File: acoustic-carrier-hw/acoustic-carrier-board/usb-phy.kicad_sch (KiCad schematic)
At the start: 64 parts, among them J9 TYPE-C-31-M-12, U18 LMV321, U6 TS3USB30EDGSR, U7 USB3300-EZK, Y3 Crystal_GND24_Small

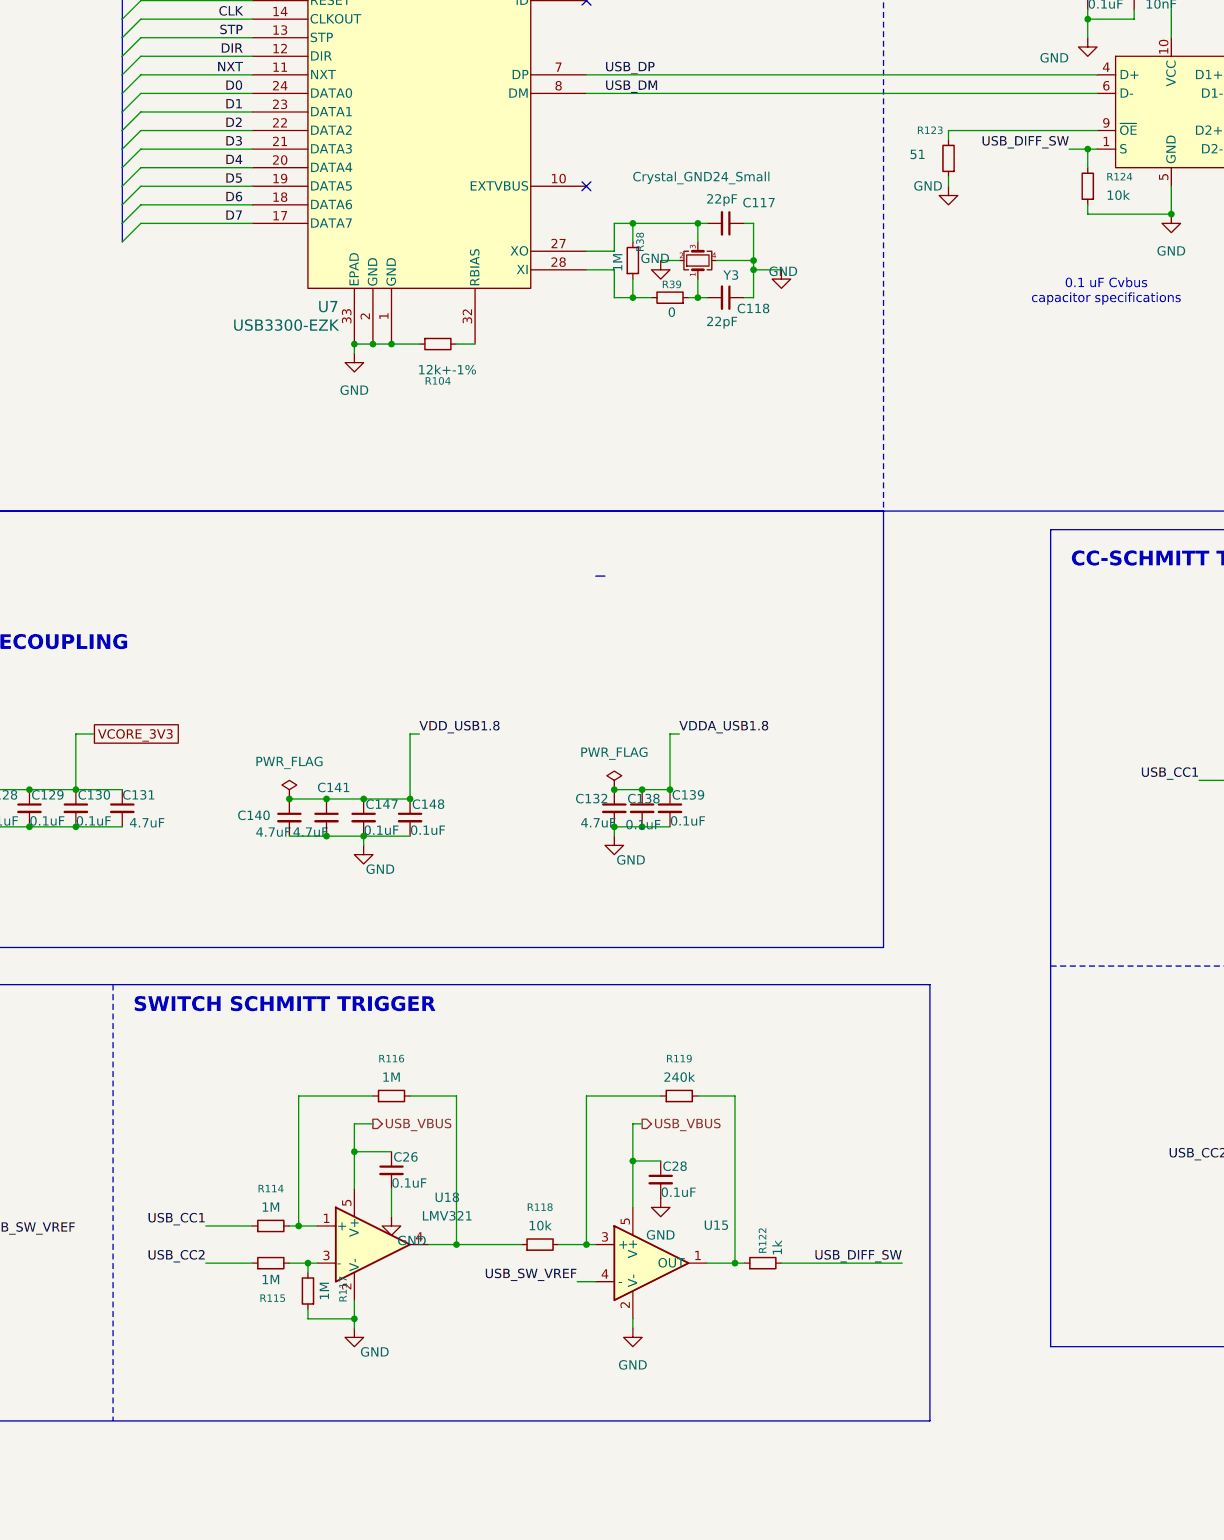
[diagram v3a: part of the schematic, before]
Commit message: [¢arrier] Finished checks, startting with layout and routing
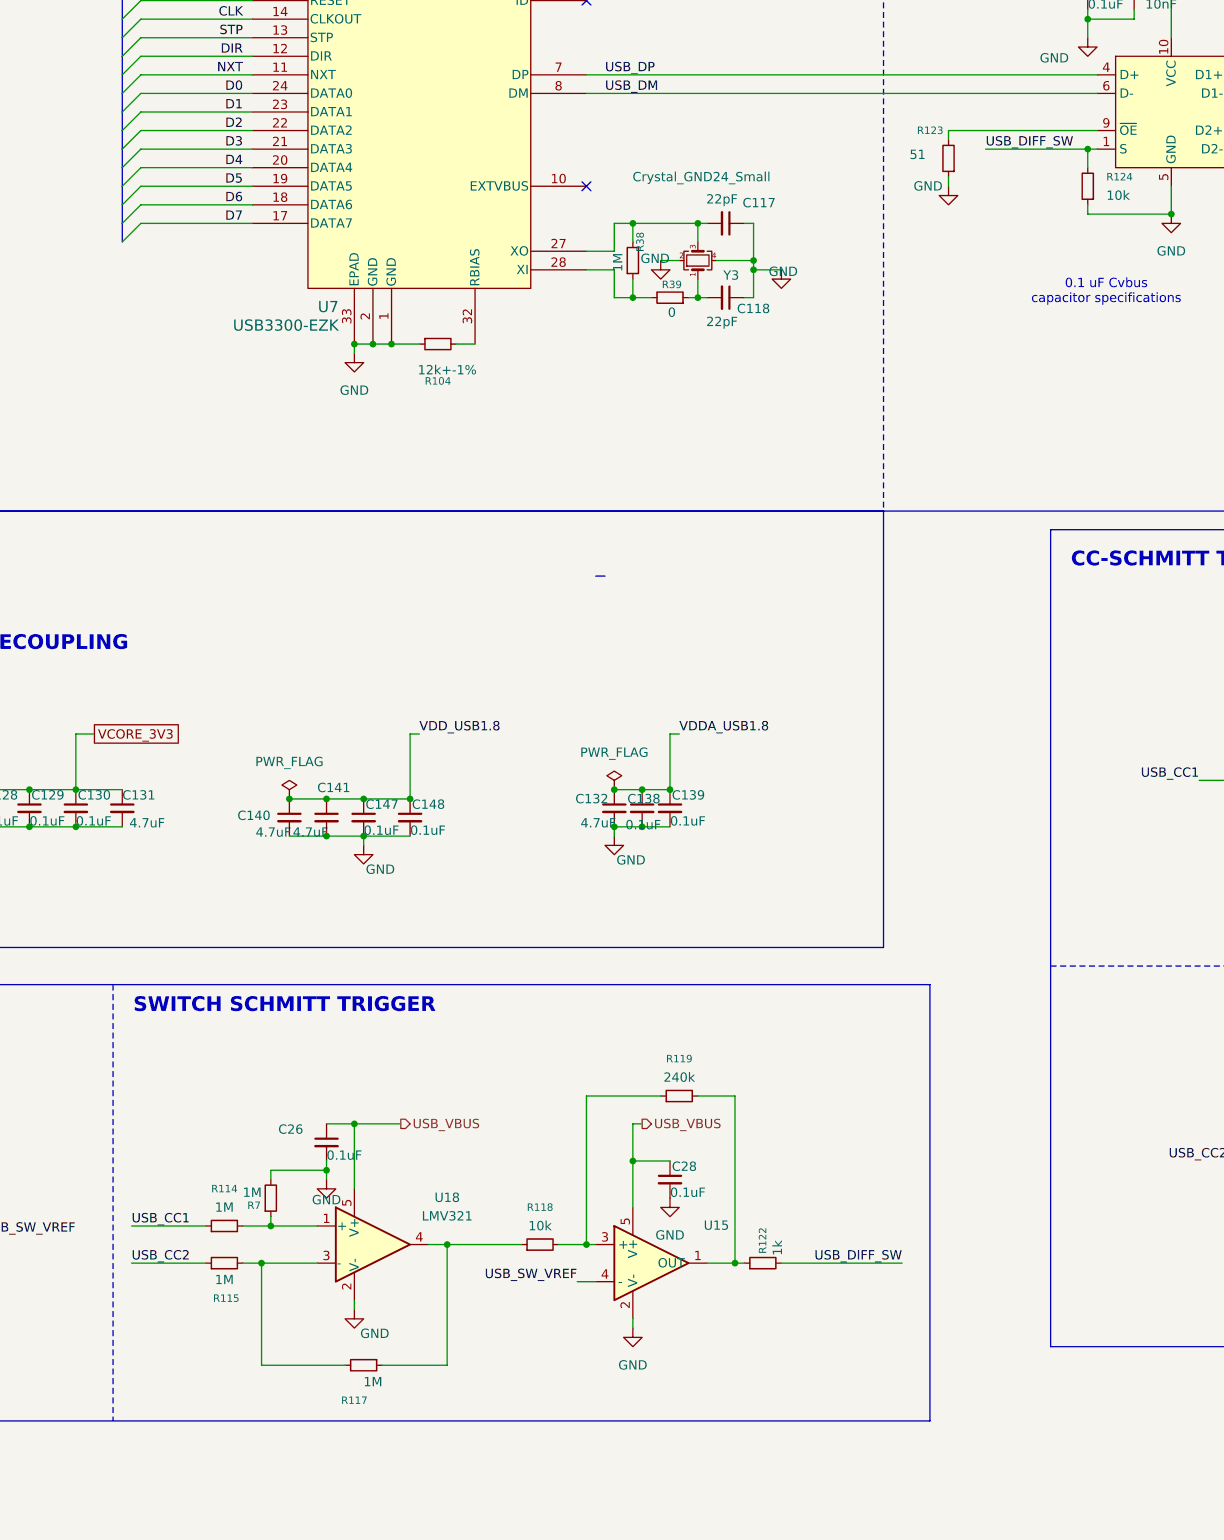
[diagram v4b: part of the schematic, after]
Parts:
- removed R116: 1M, Resistor_SMD:R_0603_1608Metric_Pad0.98x0.95mm_HandSolder, symbol Device:R_Small
- added R7: 1M, Resistor_SMD:R_0603_1608Metric_Pad0.98x0.95mm_HandSolder, symbol Device:R_Small
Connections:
- net GND: now also R7.2; no longer R117.1
- net at R114.2, U18.1 (+): now also R7.1
- net at R118.1, U18.4: now also R117.1
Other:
- moved on the sheet: C26, C28, R114, R115, R117

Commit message: [carrier] Did some check for example schematics, starting layout
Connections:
- net USBDN1 renamed USB_DN1
- net USBDN2 renamed USB_DN2
- net USBDP1 renamed USB_DP1
- net USBDP2 renamed USB_DP2
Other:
- note added: "USB3300 ID PIN: - internally pulled HIGH (peripheral function, USB-B) DP - Termination included where necessary"
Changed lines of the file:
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@@
 		)
 	)
+	(text "USB3300\nID PIN: \n- internally pulled HIGH (peripheral function, USB-B)\nDP\n- Termination included where necessary"
+		(exclude_from_sim no)
+		(at 81.28 38.608 0)
+		(effects
+			(font
+				(size 1.27 1.27)
+			)
+			(justify left bottom)
+		)
+	)
 	(text "USB_CC1: high -> USB_DIFF_SW: high -> D2 ACTIVE\nUSB_CC2: high -> USB_DIFF_SW: low -> D1 ACTIVE"
 		(exclude_from_sim no)
@@
 	)
 	(junction
+		(at 144.78 38.1)
+		(diameter 0)
+		(color 0 0 0 0)
+	)
+	(junction
 		(at 182.88 172.72)
 		(diameter 0)
@@
 	(wire
 		(pts
+			(xy 130.81 38.1) (xy 144.78 38.1)
+		)
+		(stroke
+			(width 0)
+			(type default)
+		)
+	)
+	(wire
+		(pts
 			(xy 88.9 240.03) (xy 88.9 243.84)
 		)
@@
 	(wire
 		(pts
+			(xy 130.81 60.96) (xy 130.81 38.1)
+		)
+		(stroke
+			(width 0)
+			(type default)
+		)
+	)
+	(wire
+		(pts
 			(xy 313.69 82.55) (xy 332.74 82.55)
 		)
@@
 	(wire
 		(pts
-			(xy 133.35 60.96) (xy 129.54 60.96)
+			(xy 133.35 60.96) (xy 130.81 60.96)
 		)
 		(stroke
@@
 		)
 	)
-	(label "USBDP1"
+	(label "USB_DP1"
 		(at 325.12 80.01 0)
 		(effects
@@
 		)
 	)
-	(label "USBDN2"
+	(label "USB_DN2"
 		(at 325.12 77.47 0)
 		(effects
@@
 		)
 	)
-	(label "USBDN1"
+	(label "USB_DN1"
 		(at 325.12 82.55 0)
 		(effects
@@
 		)
 	)
-	(label "USBDP2"
+	(label "USB_DP2"
 		(at 325.12 74.93 0)
 		(effects
@@
 				(hide yes)
 			)
-		)
-	)
-	(global_label "VCORE_3V3"
-		(shape passive)
-		(at 129.54 60.96 180)
-		(fields_autoplaced yes)
-		(effects
-			(font
-				(size 1.27 1.27)
-			)
-			(justify right)
-		)
-		(property "Intersheetrefs" "${INTERSHEET_REFS}"
-			(at 117.0828 60.96 0)
-			(effects
-				(font
-					(size 1.27 1.27)
-				)
-				(justify right)
-				(hide yes)
-			)

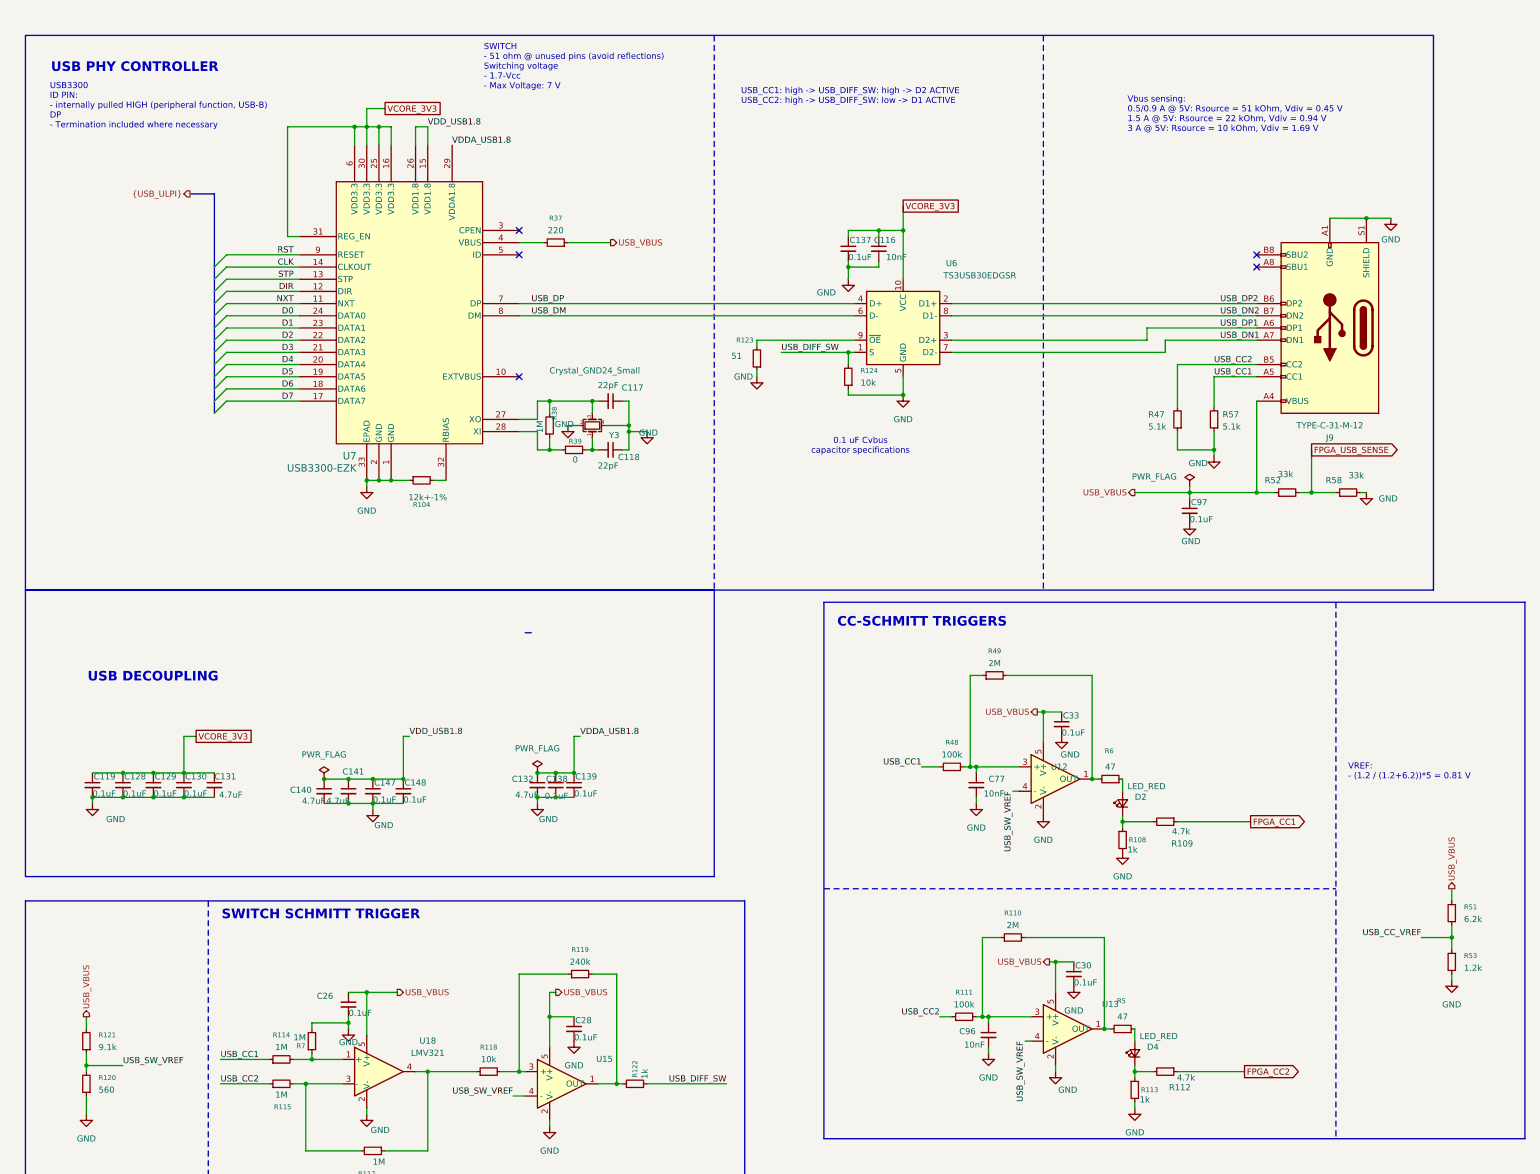
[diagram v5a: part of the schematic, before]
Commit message: [carrier] Added testpoints
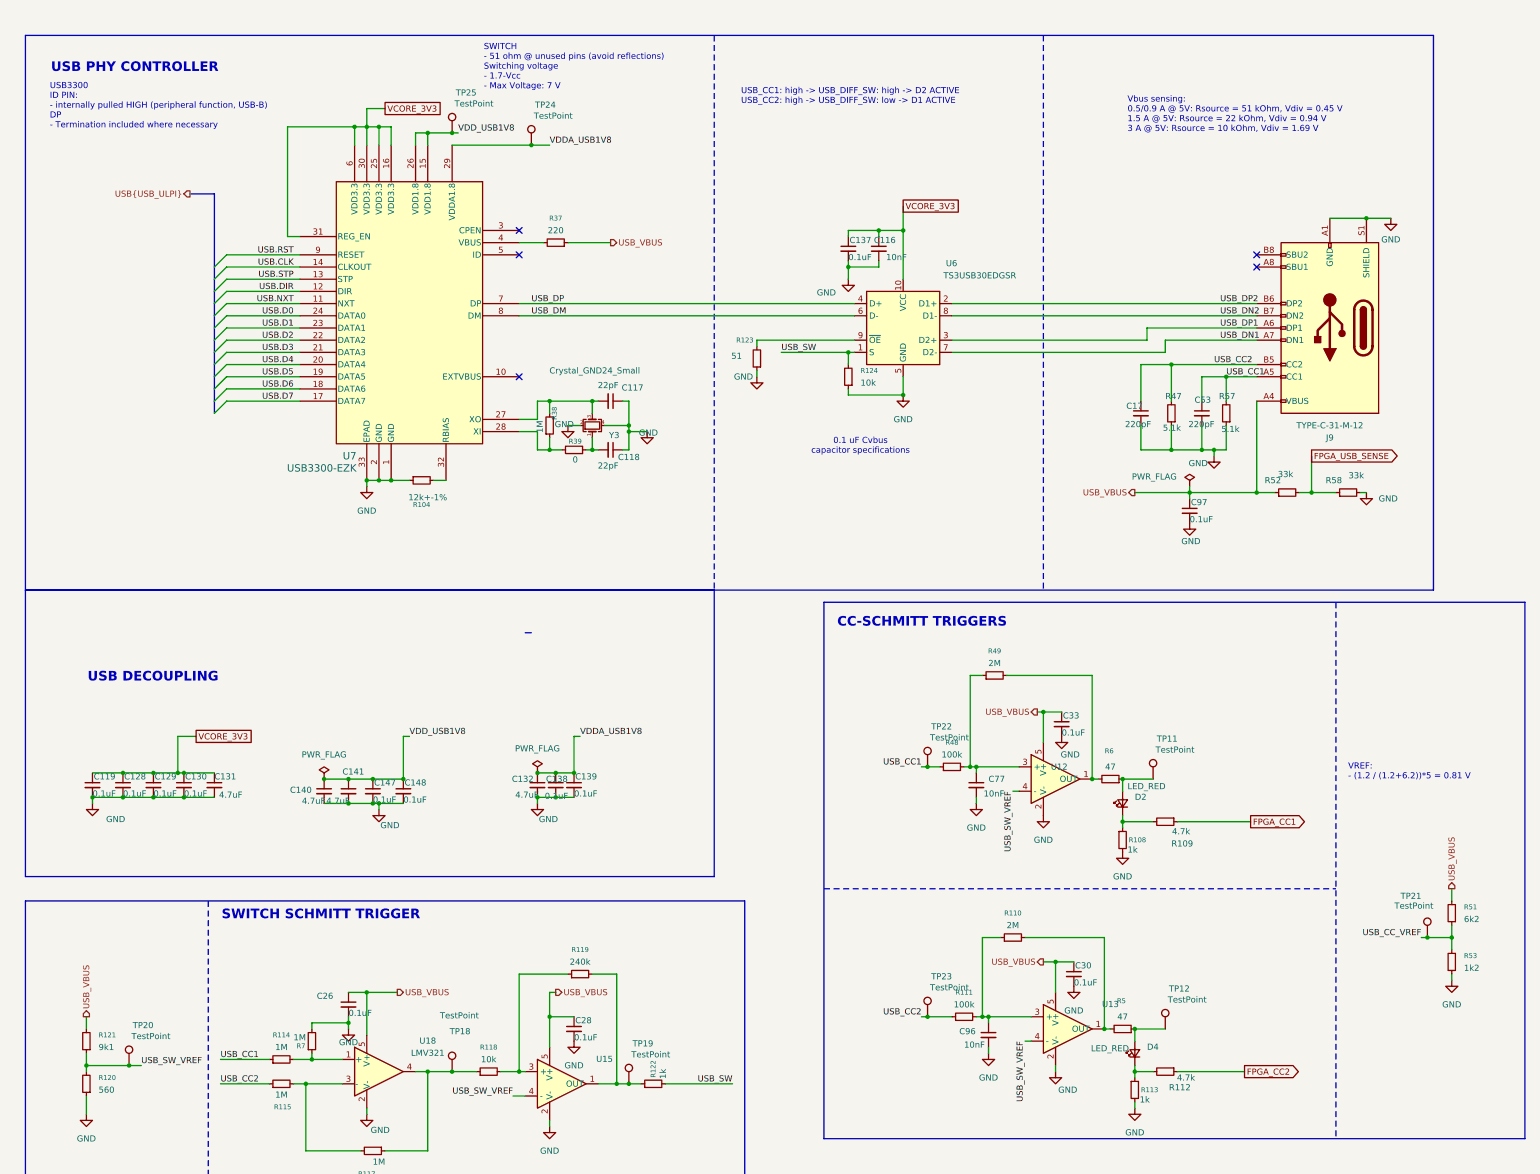
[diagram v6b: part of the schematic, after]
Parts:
- added C17, C53: 220pF, Capacitor_SMD:C_0402_1005Metric, symbol Device:C_Small
- added TP11, TP12, TP18, TP19, TP20, TP21, TP22, TP23, TP24, TP25: TestPoint, TestPoint:TestPoint_Loop_D1.80mm_Drill1.0mm_Beaded, symbol Connector:TestPoint
- C116, C77, C96: LPN CL05B103KB5NNNC -> C15195; MPN C15195 -> CL05B103KB5NNNC
- R108, R113, R122: MPN 0603WAF1001T5E -> 0603WAF1001T5E
- R109, R112: footprint Resistor_SMD:R_0402_1005Metric -> Resistor_SMD:R_0603_1608Metric; LPN 0603WAF4701T5E -> C23162; MPN C23162 -> 0603WAF4701T5E
- R121: value 9.1k -> 9k1
- R47, R57: footprint Resistor_SMD:R_0805_2012Metric -> Resistor_SMD:R_0603_1608Metric; LPN C27834 -> C23186; MPN (none) -> 0603WAF5101T5E
- R51: value 6.2k -> 6k2
- R53: value 1.2k -> 1k2
- R58: MPN (none) -> 0603WAF3302T5E
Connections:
- net GND: now also C17.2, C53.2
- net USB_CC1: now also C53.1, TP22.1
- net USB_CC2: now also C17.1, TP23.1
- net USB_CC_VREF: now also TP21.1
- net USB_SW_VREF: now also TP20.1
- net at D2.2 (A), R6.1: now also TP11.1
- net at R117.1, R118.1, U18.4: now also TP18.1
- net at D4.2 (A), R5.1: now also TP12.1
- net at R119.2, R122.1, U15.1 (OUT): now also TP19.1
- net CLK renamed USB.CLK
- net D0 renamed USB.D0
- net D1 renamed USB.D1
- net D2 renamed USB.D2
- net D3 renamed USB.D3
- net D4 renamed USB.D4
- net D5 renamed USB.D5
- net D6 renamed USB.D6
- net D7 renamed USB.D7
- net DIR renamed USB.DIR
- net NXT renamed USB.NXT
- net RST renamed USB.RST
- net STP renamed USB.STP
- net USB_DIFF_SW renamed USB_SW
- net VDDA_USB1.8 renamed VDDA_USB1V8
- net VDDA_USB1V8: now also TP24.1
- net VDD_USB1.8 renamed VDD_USB1V8
- net VDD_USB1V8: now also TP25.1
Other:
- moved on the sheet: R122, R47, R57
